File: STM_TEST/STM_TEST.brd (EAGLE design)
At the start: 100 x 80 mm, 25 parts, among them U1 TPS2115APWR, Y2 ECS-80-S-4X

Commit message: Routing and Stuff
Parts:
- removed LED: (no value), SparkFun-Resistors:0603
- added C3, C4: 1.0uF, SparkFun-Capacitors:0603
- added D1: (no value), SparkFun-LED:LED-0603
- added J1: (no value), SparkFun-Connectors:1X02
- added R4: 100k, SparkFun-Resistors:0603
- added SW1, SW2: (no value), special:EDG-02
- added U2: AZ1117EH-3.3TRG1, AZ1117EH-3.3TRG1:SOT230P700X180-4N
- moved CR1 61.2 mm to (17.4, 40.7)
- moved C12 53.0 mm to (46.7, 13.1)
- moved C15 53.0 mm to (50.0, 12.1)
- moved C18 53.0 mm to (41.3, 20.1)
- moved R7 53.0 mm to (38.4, 10.2)
- moved R8 53.0 mm to (40.4, 17.5)
- moved R9 53.0 mm to (38.4, 13.6)
- moved RESET1 53.0 mm to (38.2, 22.5)
- moved SV2 53.0 mm to (47.8, 23.6)
- moved C13 53.0 mm to (49.3, 8.51)
- moved C14 53.0 mm to (46.7, 11.4)
- moved C16 53.0 mm to (47.6, 8.51)
- moved C17 53.0 mm to (46.0, 8.51)
- moved C19 53.0 mm to (32.9, 15.1)
- moved C20 53.0 mm to (32.9, 8.51)
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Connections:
- removed net N$1: R3.2, U1.3
- new net +3V3BU: SW2.1, U1.7
- new net D0: R3.2, SW1.1, U1.2
- new net D1: R4.2, SW1.2, U1.3
- new net VCC: C3.1, J1.2, U2.3
- net +3V3: now also SW2.3, SW2.4; no longer U1.7
- net +3V3ROV: now also C4.1, R4.1, SW2.2, U2.2, U2.4
- net GND: now also C3.2, C4.2, D1.C, J1.1, SW1.3, SW1.4, U2.1; no longer LED.1, U1.2
- net N$3: now also D1.A; no longer LED.2
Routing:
- net +3V3: track 15.3 -> 46.7 mm
- net +3V3BU: track 0.00 -> 23.5 mm, vias 0 -> 1
- net +3V3BAT: track 0.00 -> 16.7 mm, vias 0 -> 1
- net D0: track 0.00 -> 9.68 mm
- net D1: track 0.00 -> 9.35 mm, vias 0 -> 2
- net +3V3ROV: track 0.00 -> 8.97 mm, vias 0 -> 2
- net VCC: track 0.00 -> 8.42 mm, vias 0 -> 1
- net N$2: track 0.00 -> 2.38 mm
- net N$3: track 0.00 -> 2.01 mm
- net N$7: track 3.76 -> 5.54 mm
- added copper zone on layer 1, net +3V3ROV
- added copper zone on layer 1, net GND
- added copper zone on layer 16, net GND

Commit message: More Stuff
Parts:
- moved CR1 54.2 mm to (57.6, 4.29), turned to 180 degrees
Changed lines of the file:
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@@
 <?xml version="1.0" encoding="utf-8"?>
 <!DOCTYPE eagle SYSTEM "eagle.dtd">
-<eagle version="9.2.0">
+<eagle version="8.6.1">
 <drawing>
 <settings>
@@
 <param name="checkStop" value="0"/>
 <param name="checkValues" value="0"/>
-<param name="checkNames" value="1"/>
-<param name="checkWireStubs" value="1"/>
-<param name="checkPolygonWidth" value="0"/>
 <param name="useDiameter" value="13"/>
 <param name="maxErrors" value="50"/>
@@
 <attribute name="VALUE" x="9.906" y="16.5608" size="0.6096" layer="28" font="vector" ratio="20" rot="MR180" align="top-center"/>
 </element>
-<element name="CR1" library="M95256" package="SO-8" value="M95256-WMN6TP" x="17.367" y="40.673">
-<attribute name="MANUFACTURER_PART_NUMBER" value="M95256WMN6TP" x="17.367" y="40.673" size="1.778" layer="27" display="off"/>
-<attribute name="NAME" x="14.0904" y="40.038" size="1.27" layer="25" ratio="6" rot="SR0"/>
-<attribute name="VENDOR" value="STMicroelectronics" x="17.367" y="40.673" size="1.778" layer="27" display="off"/>
+<element name="CR1" library="M95256" package="SO-8" value="M95256-WMN6TP" x="57.563" y="4.285" rot="R180">
+<attribute name="MANUFACTURER_PART_NUMBER" value="M95256WMN6TP" x="57.563" y="4.285" size="1.778" layer="27" rot="R180" display="off"/>
+<attribute name="NAME" x="60.8396" y="4.92" size="1.27" layer="25" ratio="6" rot="SR180"/>
+<attribute name="VENDOR" value="STMicroelectronics" x="57.563" y="4.285" size="1.778" layer="27" rot="R180" display="off"/>
 </element>
 <element name="R1" library="SparkFun-Resistors" library_urn="urn:adsk.eagle:library:532" package="0603" package3d_urn="urn:adsk.eagle:package:39650/1" value="400" x="14.944" y="3.99">
@@
 <wire x1="45.886" y1="13.081" x2="52.832" y2="23.622" width="0" layer="19" extent="16-16"/>
 <wire x1="25.804" y1="8.52" x2="25.804" y2="5.98" width="0" layer="19" extent="1-1"/>
-<wire x1="20.0467" y1="42.578" x2="41.236" y2="17.526" width="0" layer="19" extent="1-1"/>
+<wire x1="54.8833" y1="2.38" x2="41.236" y2="17.526" width="0" layer="19" extent="1-1"/>
 </signal>
 <signal name="NRST">
@@
 </signal>
 </signals>
-<mfgpreviewcolors>
-<mfgpreviewcolor name="soldermaskcolor" color="0xC8008000"/>
-<mfgpreviewcolor name="silkscreencolor" color="0xFFFEFEFE"/>
-<mfgpreviewcolor name="backgroundcolor" color="0xFF282828"/>
-<mfgpreviewcolor name="coppercolor" color="0xFFFFBF00"/>
-<mfgpreviewcolor name="substratecolor" color="0xFF786E46"/>
-</mfgpreviewcolors>
 </board>
 </drawing>

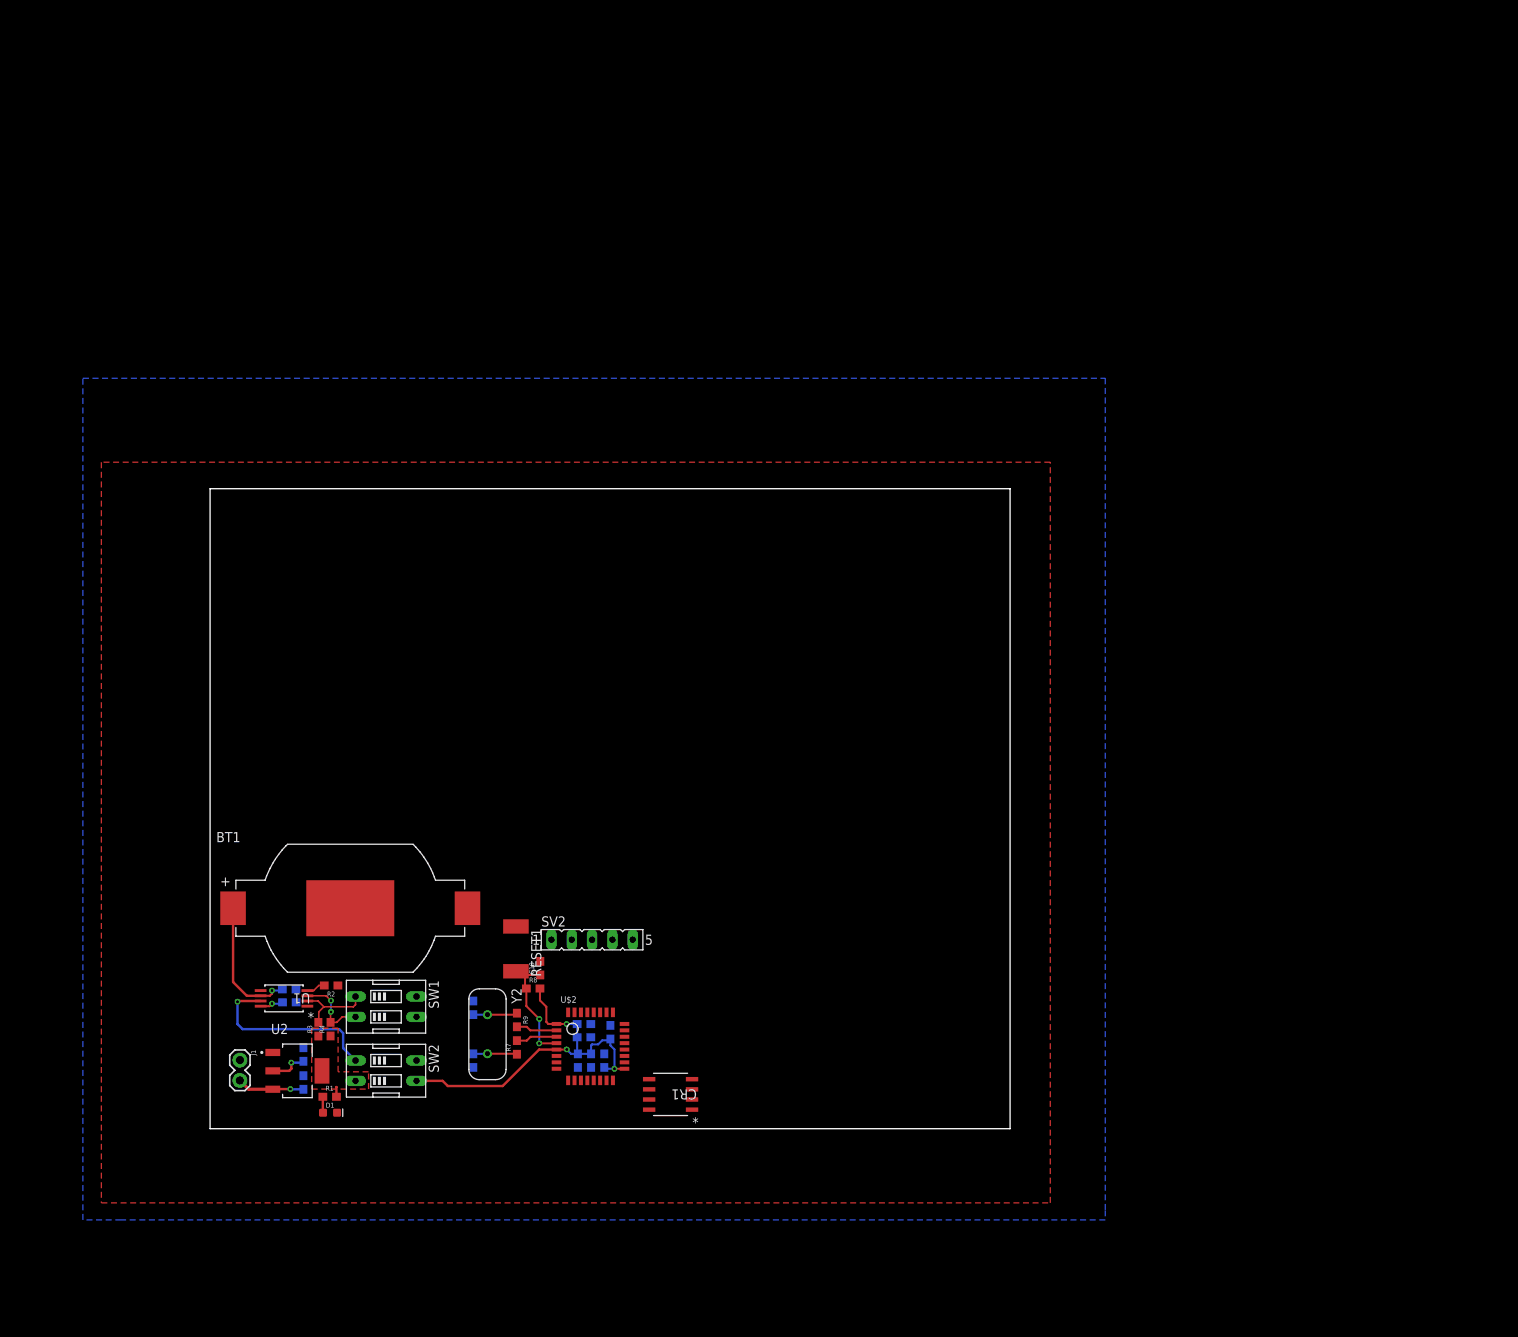
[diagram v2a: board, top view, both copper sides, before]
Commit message: Board Dimensions and Connector Layout
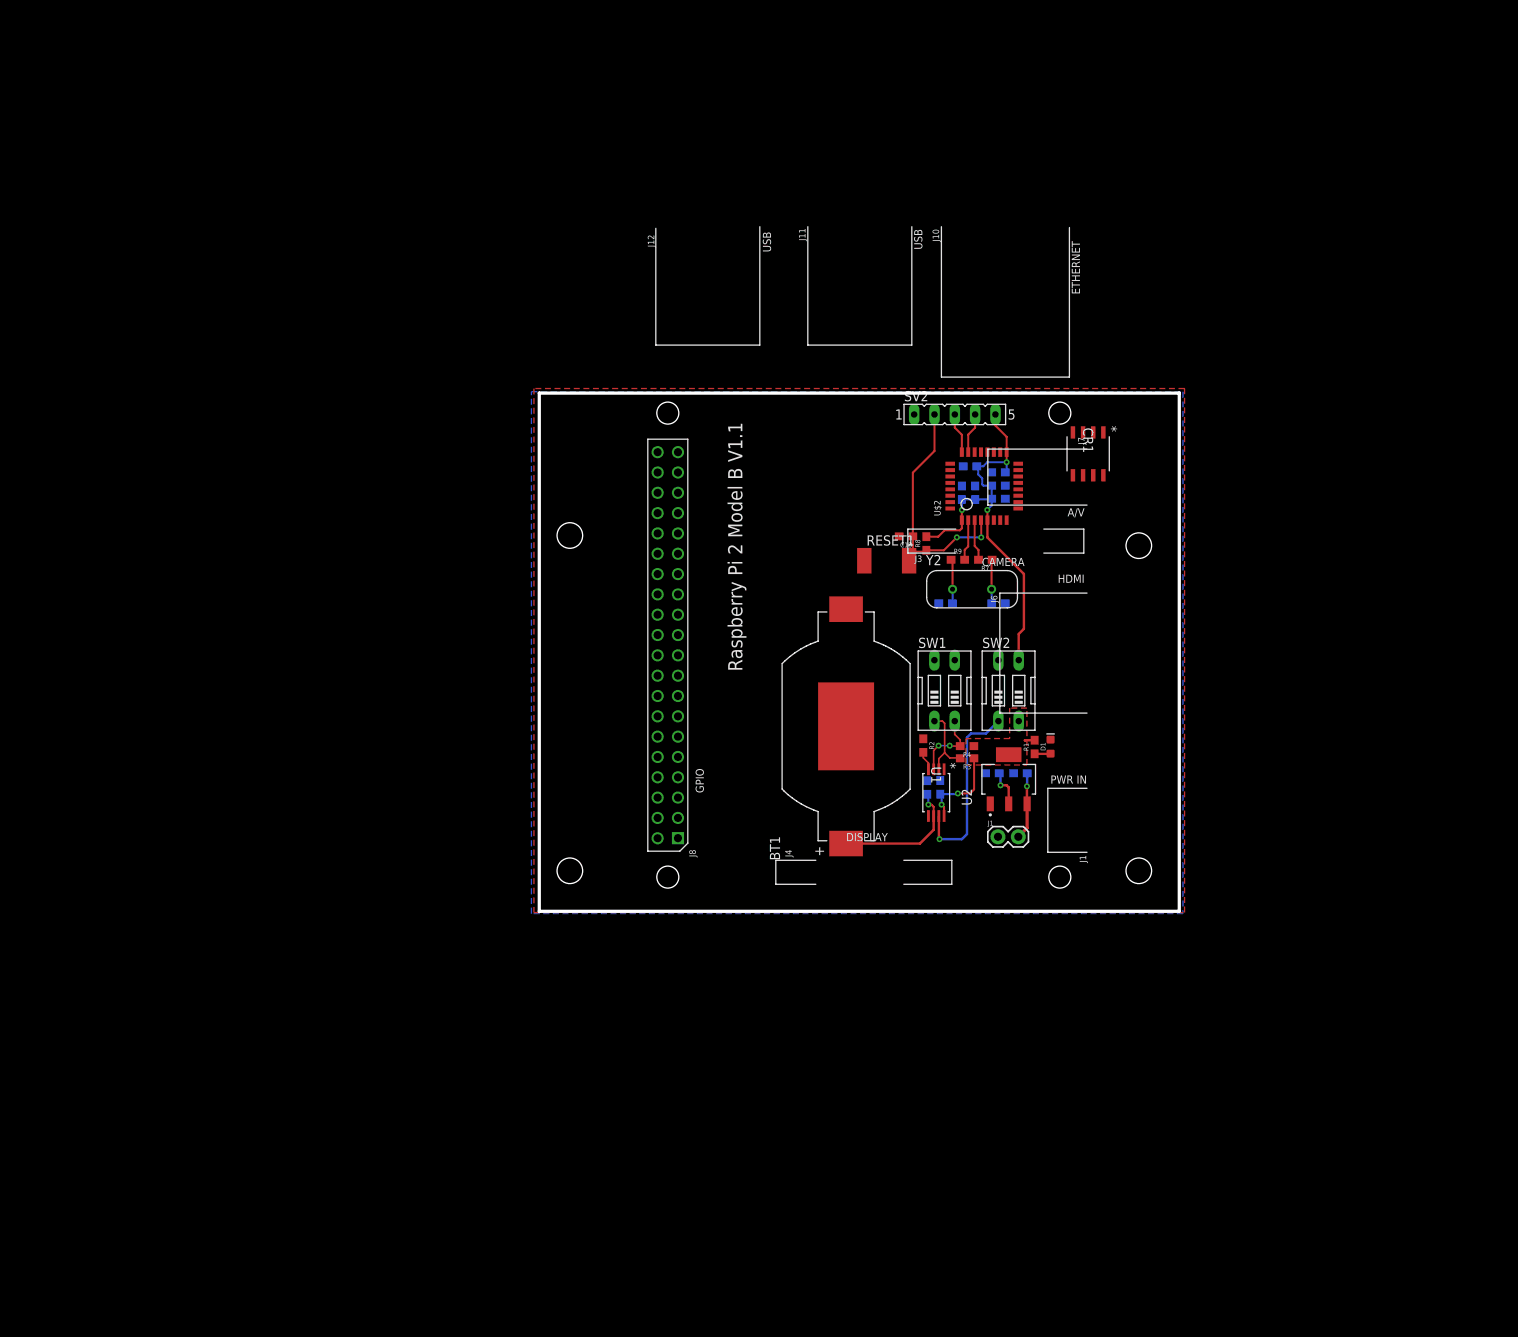
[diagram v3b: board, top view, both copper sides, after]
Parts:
- added PCB1: RPI2, MicrocontrollerComponents:RPI2
- R3, R4: value 100k -> 10k
- moved D1 101.0 mm to (105.1, 47.8), turned to 90 degrees
- moved J1 98.8 mm to (98.5, 36.5), turned to 0 degrees
- moved R1 98.4 mm to (103.1, 47.7), turned to 90 degrees
- moved C3 97.6 mm to (101.3, 44.4), turned to 0 degrees
- moved U2 96.1 mm to (99.8, 43.7), turned to 90 degrees
- moved CR1 95.6 mm to (109.8, 84.4), turned to 270 degrees
- moved C4 93.0 mm to (97.8, 44.4), turned to 0 degrees
- moved SW2 91.2 mm to (99.8, 54.8), turned to 0 degrees
- moved U$2 88.7 mm to (99.6, 76.1), turned to 90 degrees
- moved C13 88.5 mm to (98.6, 82.0), turned to 0 degrees
- moved C16 88.1 mm to (98.6, 80.4), turned to 180 degrees
- moved R3 87.9 mm to (94.6, 46.3), turned to 180 degrees
- moved C17 87.7 mm to (98.6, 78.7), turned to 180 degrees
- moved R4 87.1 mm to (94.6, 47.8), turned to 180 degrees
- moved C20 87.0 mm to (98.6, 65.7), turned to 180 degrees
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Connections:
- new net +5V: PCB1.P$2, PCB1.P$4
- new net CE0: PCB1.P$24
- new net MISO: PCB1.P$21
- new net MOSI: PCB1.P$19
- new net RESET: PCB1.P$7
- new net SCLK: PCB1.P$23
- net GND: now also PCB1.P$14, PCB1.P$20, PCB1.P$25, PCB1.P$30, PCB1.P$34, PCB1.P$39, PCB1.P$6, PCB1.P$9
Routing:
- net NRST: track 14.7 -> 31.1 mm
- net +3V3ROV: track 8.97 -> 17.4 mm, vias 2 -> 3
- net +3V3: track 46.7 -> 52.0 mm
- net SWCLK: track 0.00 -> 5.07 mm
- net SWDIO: track 0.00 -> 5.07 mm
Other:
- board size 100 x 80 mm -> 80 x 64.8 mm

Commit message: Y'all Like Samtech?
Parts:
- added R5, R6: 100k, SparkFun-Resistors:0603
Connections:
- net SCLK renamed SCLK_PI
- new net CAN_RX: U$2.PA11
- new net CAN_TX: U$2.PA12
- new net CS1: CR1.1, R5.2
- new net I2C1_SCL: U$2.PA9
- new net I2C1_SDA: U$2.PA10
- new net MISO_PI: PCB1.P$21
- new net MOSI_PI: PCB1.P$19
- new net SCK: CR1.6, R6.1, U$2.PA5
- new net SCL: PCB1.P$5
- new net SDA: PCB1.P$3
- new net UART_RXD: PCB1.P$10
- new net UART_TXD: PCB1.P$8
- net +3V3: now also R5.1
- net GND: now also R6.2
- net MISO: now also CR1.5, U$2.PA6; no longer PCB1.P$21
- net MOSI: now also CR1.2, U$2.PA7; no longer PCB1.P$19
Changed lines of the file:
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@@
 <?xml version="1.0" encoding="utf-8"?>
 <!DOCTYPE eagle SYSTEM "eagle.dtd">
-<eagle version="9.2.0">
+<eagle version="8.6.1">
 <drawing>
 <settings>
@@
 <param name="checkStop" value="0"/>
 <param name="checkValues" value="0"/>
-<param name="checkNames" value="1"/>
-<param name="checkWireStubs" value="1"/>
-<param name="checkPolygonWidth" value="0"/>
 <param name="useDiameter" value="13"/>
 <param name="maxErrors" value="50"/>
@@
 </element>
 <element name="PCB1" library="MicrocontrollerComponents" package="RPI2" value="RPI2" x="109.717" y="27.951" rot="R90"/>
+<element name="R5" library="SparkFun-Resistors" library_urn="urn:adsk.eagle:library:532" package="0603" package3d_urn="urn:adsk.eagle:package:39650/1" value="100k" x="43" y="25">
+<attribute name="PROD_ID" value="RES-07856" x="43" y="25" size="1.778" layer="27" display="off"/>
+</element>
+<element name="R6" library="SparkFun-Resistors" library_urn="urn:adsk.eagle:library:532" package="0603" package3d_urn="urn:adsk.eagle:package:39650/1" value="100k" x="43" y="21">
+<attribute name="PROD_ID" value="RES-07856" x="43" y="21" size="1.778" layer="27" display="off"/>
+</element>
 </elements>
 <signals>
@@
 <contactref element="PCB1" pad="P$39"/>
 <contactref element="PCB1" pad="P$25"/>
+<contactref element="R6" pad="2"/>
+<wire x1="101.018" y1="83.123" x2="107.856" y2="87.0397" width="0" layer="19" extent="1-1"/>
+<wire x1="99.402" y1="80.391" x2="101.018" y2="83.123" width="0" layer="19" extent="1-16"/>
+<wire x1="99.402" y1="78.74" x2="99.402" y2="80.391" width="0" layer="19" extent="16-16"/>
+<wire x1="97.702" y1="82.042" x2="99.402" y2="80.391" width="0" layer="19" extent="16-16"/>
+<wire x1="95.631" y1="80.352" x2="97.702" y2="82.042" width="0" layer="19" extent="16-16"/>
+<wire x1="93.98" y1="80.352" x2="95.631" y2="80.352" width="0" layer="19" extent="16-16"/>
+<wire x1="94.146" y1="82.804" x2="93.98" y2="80.352" width="0" layer="19" extent="16-16"/>
+<wire x1="92.518" y1="78.323" x2="93.98" y2="80.352" width="0" layer="19" extent="1-16"/>
+<wire x1="92.518" y1="77.523" x2="92.518" y2="78.323" width="0" layer="19" extent="1-1"/>
+<wire x1="86.145" y1="74.041" x2="92.518" y2="77.523" width="0" layer="19" extent="1-1"/>
+<wire x1="81.782" y1="70.993" x2="86.145" y2="74.041" width="0" layer="19" extent="1-1"/>
+<wire x1="79.502" y1="64.942" x2="81.782" y2="70.993" width="0" layer="19" extent="1-1"/>
+<wire x1="88.011" y1="89.281" x2="94.146" y2="82.804" width="0" layer="19" extent="16-16"/>
+<wire x1="91.098" y1="65.659" x2="86.145" y2="74.041" width="0" layer="19" extent="1-16"/>
+<wire x1="90.541" y1="58.57" x2="91.098" y2="65.659" width="0" layer="19" extent="16-16"/>
+<wire x1="93.081" y1="58.57" x2="90.541" y2="58.57" width="0" layer="19" extent="1-1"/>
+<wire x1="99.402" y1="65.659" x2="91.098" y2="65.659" width="0" layer="19" extent="16-16"/>
+<wire x1="89.155" y1="48.741" x2="90.541" y2="58.57" width="0" layer="19" extent="1-1"/>
+<wire x1="89.645" y1="43.5" x2="89.155" y2="48.741" width="0" layer="19" extent="1-16"/>
+<wire x1="91.2622" y1="43.522" x2="89.645" y2="43.5" width="0" layer="19" extent="16-16"/>
+<wire x1="89.796" y1="39.085" x2="89.645" y2="43.5" width="0" layer="19" extent="1-16"/>
+<wire x1="96.934" y1="44.43" x2="91.2622" y2="43.522" width="0" layer="19" extent="16-16"/>
+<wire x1="100.434" y1="44.432" x2="96.934" y2="44.43" width="0" layer="19" extent="16-16"/>
+<wire x1="97.53" y1="40.606" x2="96.934" y2="44.43" width="0" layer="19" extent="1-16"/>
+<wire x1="98.488" y1="36.493" x2="97.53" y2="40.606" width="0" layer="19" extent="1-1"/>
+<wire x1="105.061" y1="48.637" x2="100.434" y2="44.432" width="0" layer="19" extent="1-16"/>
+<wire x1="58.4852" y1="66.7876" x2="79.502" y2="64.942" width="0" layer="19" extent="1-1"/>
+<wire x1="55.9452" y1="71.8676" x2="58.4852" y2="66.7876" width="0" layer="19" extent="1-1"/>
+<wire x1="55.9452" y1="76.9476" x2="55.9452" y2="71.8676" width="0" layer="19" extent="1-1"/>
+<wire x1="58.4852" y1="84.5676" x2="55.9452" y2="76.9476" width="0" layer="19" extent="1-1"/>
+<wire x1="55.9452" y1="59.1676" x2="58.4852" y2="66.7876" width="0" layer="19" extent="1-1"/>
+<wire x1="55.9452" y1="51.5476" x2="55.9452" y2="59.1676" width="0" layer="19" extent="1-1"/>
+<wire x1="58.4852" y1="46.4676" x2="55.9452" y2="51.5476" width="0" layer="19" extent="1-1"/>
+<wire x1="55.9452" y1="41.3876" x2="58.4852" y2="46.4676" width="0" layer="19" extent="1-1"/>
+<wire x1="43.85" y1="21" x2="55.9452" y2="41.3876" width="0" layer="19" extent="1-1"/>
 </signal>
 <signal name="+3V3BAT">
@@
 <wire x1="98.171" y1="87.884" x2="99.568" y2="86.487" width="0.254" layer="1"/>
 <wire x1="99.568" y1="86.487" x2="99.568" y2="84.573" width="0.254" layer="1"/>
+<contactref element="R5" pad="1"/>
 <wire x1="99.568" y1="82.208" x2="111.666" y2="81.6803" width="0" layer="19" extent="1-16"/>
 <wire x1="98.541" y1="58.57" x2="101.081" y2="58.57" width="0" layer="19" extent="1-1"/>
+<wire x1="42.15" y1="25" x2="98.541" y2="58.57" width="0" layer="19" extent="1-1"/>
 </signal>
 <signal name="NRST">
@@
 <wire x1="90.446" y1="47.266" x2="90.446" y2="44.927" width="0.2032" layer="1"/>
 </signal>
-<signal name="SCLK">
+<signal name="SCLK_PI">
 <contactref element="PCB1" pad="P$23"/>
 </signal>
-<signal name="MISO">
+<signal name="MISO_PI">
 <contactref element="PCB1" pad="P$21"/>
 </signal>
-<signal name="MOSI">
+<signal name="MOSI_PI">
 <contactref element="PCB1" pad="P$19"/>
 </signal>
@@
 <contactref element="PCB1" pad="P$24"/>
 </signal>
+<signal name="UART_RXD">
+<contactref element="PCB1" pad="P$10"/>
+</signal>
+<signal name="UART_TXD">
+<contactref element="PCB1" pad="P$8"/>
+</signal>
+<signal name="SDA">
+<contactref element="PCB1" pad="P$3"/>
+</signal>
+<signal name="SCL">
+<contactref element="PCB1" pad="P$5"/>
+</signal>
+<signal name="MISO">
+<contactref element="U$2" pad="PA6"/>
+<contactref element="CR1" pad="5"/>
+<wire x1="101.018" y1="79.923" x2="107.856" y2="81.6803" width="0" layer="19" extent="1-1"/>
+</signal>
+<signal name="MOSI">
+<contactref element="U$2" pad="PA7"/>
+<contactref element="CR1" pad="2"/>
+<wire x1="101.018" y1="80.723" x2="110.396" y2="87.0397" width="0" layer="19" extent="1-1"/>
+</signal>
+<signal name="CAN_TX">
+<contactref element="U$2" pad="PA12"/>
+</signal>
+<signal name="CAN_RX">
+<contactref element="U$2" pad="PA11"/>
+</signal>
+<signal name="I2C1_SDA">
+<contactref element="U$2" pad="PA10"/>
+</signal>
+<signal name="I2C1_SCL">
+<contactref element="U$2" pad="PA9"/>
+</signal>
+<signal name="SCK">
+<contactref element="CR1" pad="6"/>
+<contactref element="U$2" pad="PA5"/>
+<contactref element="R6" pad="1"/>
+<wire x1="101.018" y1="79.123" x2="109.126" y2="81.6803" width="0" layer="19" extent="1-1"/>
+<wire x1="42.15" y1="21" x2="101.018" y2="79.123" width="0" layer="19" extent="1-1"/>
+</signal>
+<signal name="CS1">
+<contactref element="R5" pad="2"/>
+<contactref element="CR1" pad="1"/>
+<wire x1="43.85" y1="25" x2="111.666" y2="87.0397" width="0" layer="19" extent="1-1"/>
+</signal>
 </signals>
-<mfgpreviewcolors>
-<mfgpreviewcolor name="soldermaskcolor" color="0xC8008000"/>
-<mfgpreviewcolor name="silkscreencolor" color="0xFFFEFEFE"/>
-<mfgpreviewcolor name="backgroundcolor" color="0xFF282828"/>
-<mfgpreviewcolor name="coppercolor" color="0xFFFFBF00"/>
-<mfgpreviewcolor name="substratecolor" color="0xFF786E46"/>
-</mfgpreviewcolors>
 </board>
 </drawing>
